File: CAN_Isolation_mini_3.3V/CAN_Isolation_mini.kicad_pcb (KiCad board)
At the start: 4 copper layers, 60 x 60 mm, 58 parts, among them J1 S4B-XH-A, J10 Conn_01x04_Pin, J11 Conn_01x04_Pin, J12 Conn_01x04_Pin, J13 Conn_01x04_Pin, J14 Conn_01x04_Pin, J15 Conn_01x04_Pin, J16 Conn_01x04_Pin, J17 Conn_01x04_Pin, J2 Conn_01x04_Pin, J3 Conn_01x04_Pin, J4 Conn_01x04_Pin, J5 Conn_01x04_Pin, J6 Conn_01x04_Pin, J7 Conn_01x04_Pin, J8 Conn_01x04_Pin, J9 Conn_01x04_Pin, U1 MCP2518FDT-H/SL, U2 ISO1042QDWVRQ1, U3 MGS3123R3, U4 MGS1R51205, U5 TVS1800DRVR, U6 DTC114ECAHZGT116, U7 MGS102405, Y1 CSTNE20M0V530000R0

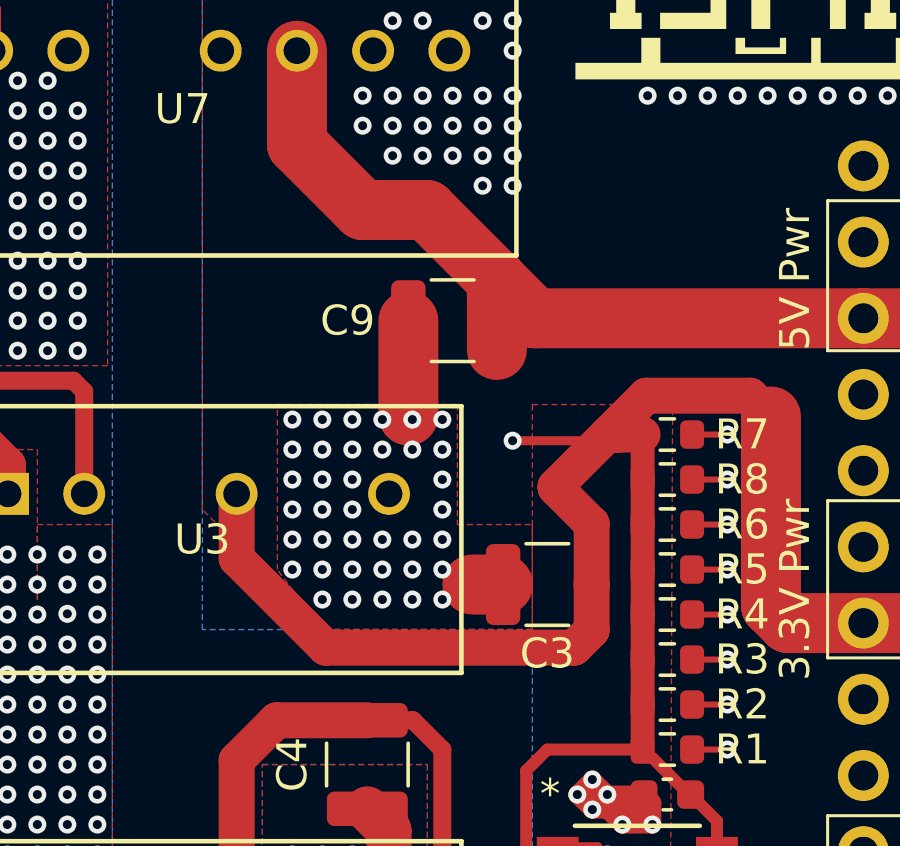
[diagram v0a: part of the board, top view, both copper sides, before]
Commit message: Fix VIA for 5&3.3V line.
Fix VIA for 5&3.3V line.
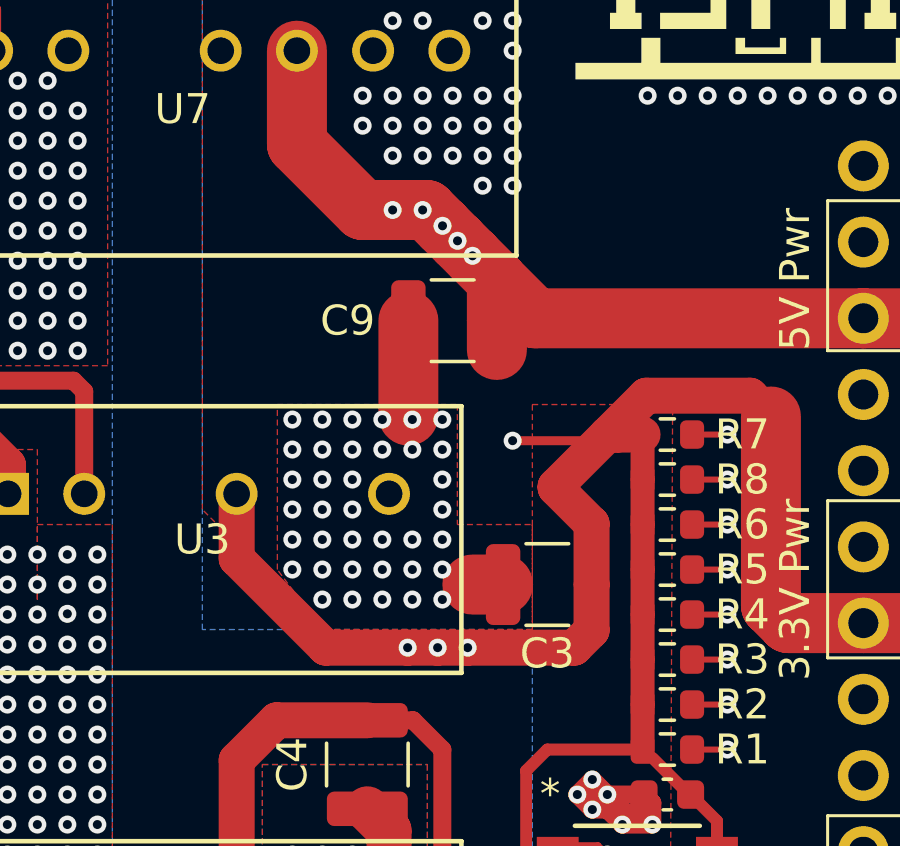
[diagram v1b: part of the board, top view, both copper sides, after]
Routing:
- net +5VP: vias 0 -> 5
- net +3.3VP: vias 2 -> 5
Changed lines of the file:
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@@
+	)
+	(segment
+		(start 124 95.398305)
+		(end 127.553695 95.398305)
+		(width 1.2)
+		(layer "F.Cu")
+		(net 51)
 	)
 	(segment
@@
 	)
 	(segment
+		(start 123 95.398305)
+		(end 124 95.398305)
+		(width 1.2)
+		(layer "F.Cu")
+		(net 51)
+	)
+	(segment
 		(start 91.657095 84.294905)
 		(end 93.657095 84.294905)
@@
 	)
 	(segment
+		(start 122 95.398305)
+		(end 123 95.398305)
+		(width 1.2)
+		(layer "F.Cu")
+		(net 51)
+	)
+	(segment
 		(start 134.110495 87.692887)
 		(end 133.417608 87)
@@
 	(segment
 		(start 119.270762 95.398305)
-		(end 127.553695 95.398305)
-		(width 1.2)
-		(layer "F.Cu")
+		(end 122 95.398305)
+		(width 1.2)
+		(layer "F.Cu")
+		(net 51)
+	)
+	(via
+		(at 122 95.398305)
+		(size 0.6)
+		(drill 0.3)
+		(layers "F.Cu" "B.Cu")
 		(net 51)
 	)
@@
 	)
 	(via
+		(at 123 95.398305)
+		(size 0.6)
+		(drill 0.3)
+		(layers "F.Cu" "B.Cu")
+		(net 51)
+	)
+	(via
 		(at 93.657095 84.294905)
 		(size 0.6)
@@
 		(net 51)
 	)
+	(via
+		(at 124 95.398305)
+		(size 0.6)
+		(drill 0.3)
+		(layers "F.Cu" "B.Cu")
+		(net 51)
+	)
 	(segment
 		(start 101.1034 72.8966)
@@
 	)
 	(segment
+		(start 124.1625 82.3375)
+		(end 124.975 83.15)
+		(width 2)
+		(layer "F.Cu")
+		(net 52)
+	)
+	(segment
 		(start 139.73 84.42)
 		(end 142.27 84.42)
@@
 	(segment
 		(start 120.5 80.81)
+		(end 121.5 80.81)
+		(width 2)
+		(layer "F.Cu")
+		(net 52)
+	)
+	(segment
+		(start 122.5 80.81)
 		(end 122.635 80.81)
 		(width 2)
@@
 	)
 	(segment
+		(start 123.1625 81.3375)
+		(end 123.6625 81.8375)
+		(width 2)
+		(layer "F.Cu")
+		(net 52)
+	)
+	(segment
 		(start 122.635 80.81)
-		(end 124.975 83.15)
+		(end 123.1625 81.3375)
+		(width 2)
+		(layer "F.Cu")
+		(net 52)
+	)
+	(segment
+		(start 123.6625 81.8375)
+		(end 124.1625 82.3375)
 		(width 2)
 		(layer "F.Cu")
@@
 	)
 	(segment
+		(start 121.5 80.81)
+		(end 122.5 80.81)
+		(width 2)
+		(layer "F.Cu")
+		(net 52)
+	)
+	(segment
 		(start 142.27 84.42)
 		(end 144.81 84.42)
@@
 		(net 52)
 	)
-	(segment
-		(start 123.58 84.42)
-		(end 123.4953 84.42)
-		(width 2)
-		(layer "In1.Cu")
-		(net 52)
-	)
-	(segment
-		(start 123.4953 84.42)
+	(via
+		(at 124.1625 82.3375)
+		(size 0.6)
+		(drill 0.3)
+		(layers "F.Cu" "B.Cu")
+		(net 52)
+	)
+	(via
+		(at 123.6625 81.8375)
+		(size 0.6)
+		(drill 0.3)
+		(layers "F.Cu" "B.Cu")
+		(net 52)
+	)
+	(via
+		(at 122.5 80.81)
+		(size 0.6)
+		(drill 0.3)
+		(layers "F.Cu" "B.Cu")
+		(net 52)
+	)
+	(via
+		(at 121.5 80.81)
+		(size 0.6)
+		(drill 0.3)
+		(layers "F.Cu" "B.Cu")
+		(net 52)
+	)
+	(via
+		(at 123.1625 81.3375)
+		(size 0.6)
+		(drill 0.3)
+		(layers "F.Cu" "B.Cu")
+		(net 52)
+	)
+	(segment
+		(start 120.53765 81.46235)
+		(end 122.54235 81.46235)
+		(width 2)
+		(layer "In1.Cu")
+		(net 52)
+	)
+	(segment
+		(start 120.53765 81.46235)
 		(end 118.31 79.2347)
 		(width 2)
@@
 	(segment
 		(start 144.81 84.42)
-		(end 123.58 84.42)
+		(end 125.5 84.42)
+		(width 2)
+		(layer "In1.Cu")
+		(net 52)
+	)
+	(segment
+		(start 122.54235 81.46235)
+		(end 125.5 84.42)
 		(width 2)
 		(layer "In1.Cu")
@@
 			(pts
 				(xy 117 74.5) (xy 119.5 74.5) (xy 119.5 78) (xy 121 79.5) (xy 123 79.5) (xy 127 83) (xy 146 83)
-				(xy 146 86) (xy 135.5 86) (xy 135.5 93) (xy 146.5 93) (xy 146.5 87.5) (xy 133 87.5) (xy 133 87.5)
-				(xy 125 87.5) (xy 123.5 86) (xy 117 86)
-			)
-		)
+				(xy 146 86) (xy 135.5 86) (xy 135.5 93) (xy 146.5 93) (xy 146.5 87.5) (xy 133 87.5) (xy 125 87.5)
+				(xy 123.5 86) (xy 117 86)
+			)
+		)
